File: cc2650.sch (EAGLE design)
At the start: 22 parts, among them IC4 CC2650MODAMOHR, SW1 SPST_TACT-KMR2, SW2 SPST_TACT-KMR2, U1 Value, U402 TPS62233DRY

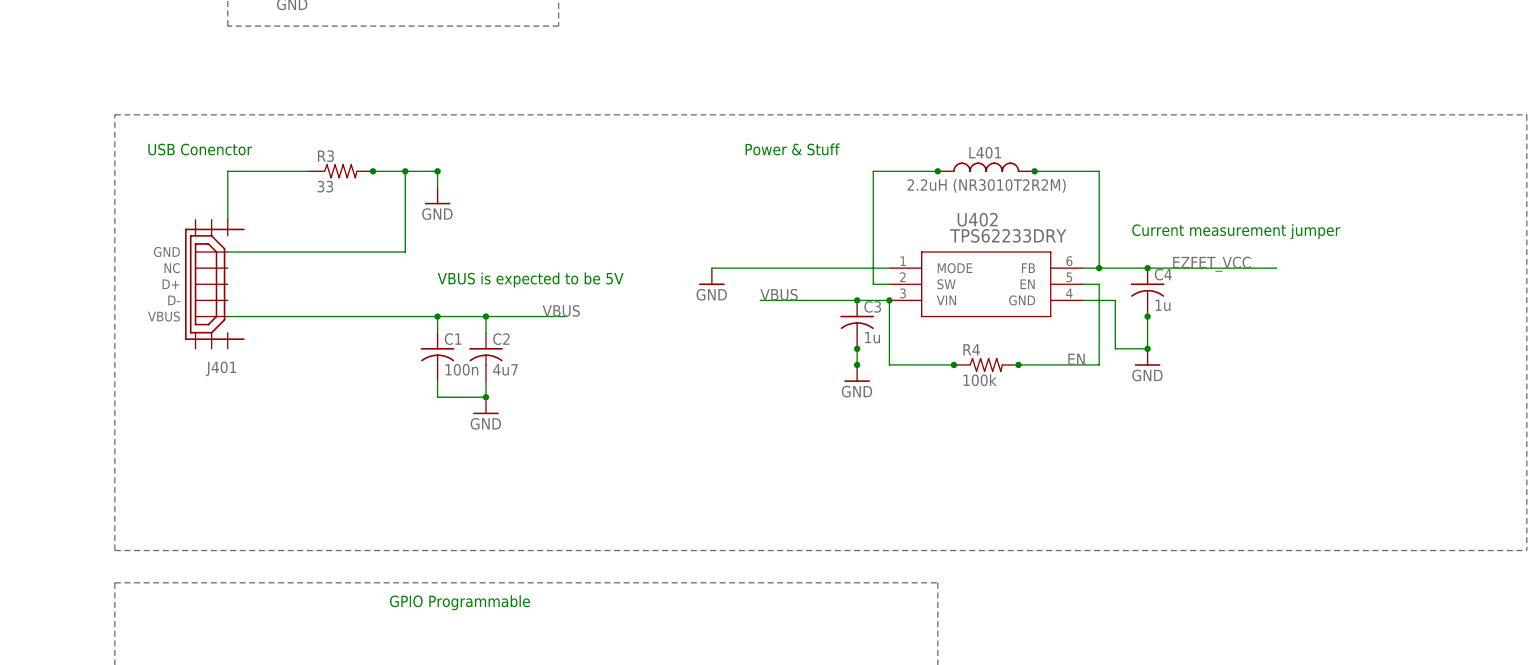
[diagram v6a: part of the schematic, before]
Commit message: Switched out USB connector.
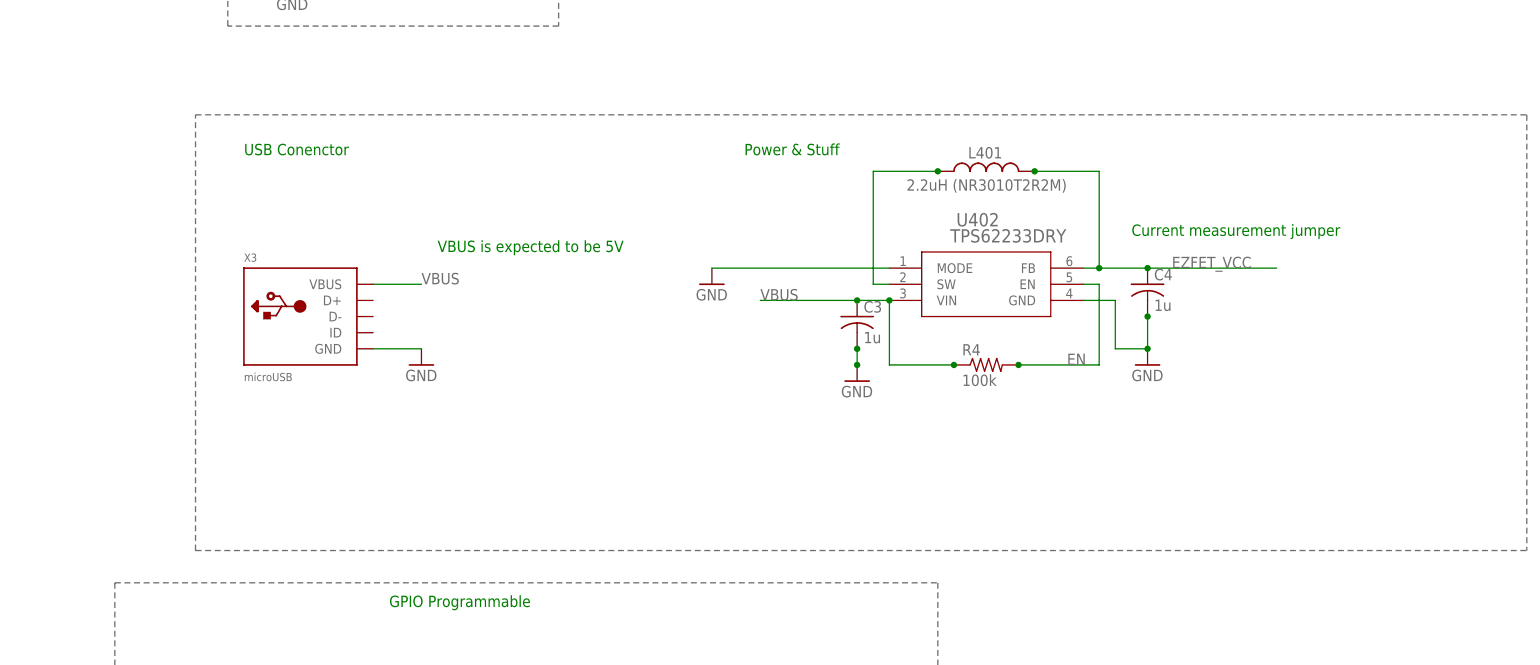
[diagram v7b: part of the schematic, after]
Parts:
- removed C1: 100n, adafruit:C-USC0402
- removed C2: 4u7, adafruit:C-USC1206
- removed J401: (no value), usb_con-update:USB_MICRO_FLIPPED
- removed R3: 33, adafruit:R-US_R0402
- added X3: microUSB, microbuilder:USB_MICRO_20329_V2
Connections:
- removed net N$1: J401.SHIELD1, R3.1
- net GND: now also X3.GND; no longer C1.2, C2.2, J401.GND, R3.2
- net VBUS: now also X3.VBUS; no longer C1.1, C2.1, J401.VBUS
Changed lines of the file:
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@@
 <attribute name="OC_NEWARK" value="05M0345"/>
 </part>
-<part name="GND56" library="supply1" deviceset="GND" device=""/>
-<part name="GND64" library="supply1" deviceset="GND" device=""/>
 <part name="U402" library="tps62231dry" deviceset="TPS6223X_DRY_6" device="" value="TPS62233DRY">
 <attribute name="MF" value=""/>
@@
 <part name="P+4" library="supply1" library_urn="urn:adsk.eagle:library:371" deviceset="VCC" device=""/>
 <part name="P+5" library="supply1" library_urn="urn:adsk.eagle:library:371" deviceset="VCC" device=""/>
-<part name="C1" library="adafruit" deviceset="C-US" device="C0402" value="100n">
-<attribute name="MF" value=""/>
-<attribute name="MPN" value="C1005X7R1H104K050BB"/>
-<attribute name="OC_NEWARK" value="04X3230"/>
-</part>
-<part name="C2" library="adafruit" deviceset="C-US" device="C1206" value="4u7">
-<attribute name="MF" value=""/>
-<attribute name="MPN" value="GRT31CC81E475KE01L"/>
-<attribute name="OC_NEWARK" value="01AC8998"/>
-</part>
 <part name="C3" library="adafruit" deviceset="C-US" device="C0805" value="1u">
 <attribute name="MF" value=""/>
@@
 <attribute name="MPN" value="CGA2B2C0G1H102J050BA"/>
 <attribute name="OC_NEWARK" value="04X3142"/>
-</part>
-<part name="R3" library="adafruit" deviceset="R-US_" device="R0402" value="33">
-<attribute name="MF" value=""/>
-<attribute name="MPN" value="ERJ-U02F33R0X"/>
-<attribute name="OC_NEWARK" value="51W3197"/>
 </part>
 <part name="R1" library="adafruit" deviceset="R-US_" device="R0402" value="47k">
@@
 </part>
 <part name="P+2" library="supply1" library_urn="urn:adsk.eagle:library:371" deviceset="VCC" device=""/>
-<part name="J401" library="usb_con-update" deviceset="USB_MICRO_FLIPPED" device="">
-<attribute name="MF" value=""/>
-<attribute name="MPN" value="ZX62R-B-5P(30)"/>
-<attribute name="OC_NEWARK" value="84Y6712"/>
-</part>
 <part name="GND6" library="supply1" library_urn="urn:adsk.eagle:library:371" deviceset="GND" device=""/>
 <part name="GND8" library="supply1" library_urn="urn:adsk.eagle:library:371" deviceset="GND" device=""/>
@@
 </part>
 <part name="U1" library="OPT3001" deviceset="OPT3001DNPR" device="" value="Value"/>
+<part name="X3" library="microbuilder" deviceset="USB" device="_MICRO_20329_V2" value="microUSB"/>
+<part name="GND4" library="supply1" library_urn="urn:adsk.eagle:library:371" deviceset="GND" device=""/>
 </parts>
 <sheets>
 <sheet>
 <plain>
-<text x="22.86" y="25.4" size="1.778" layer="91">USB Conenctor</text>
+<text x="38.1" y="25.4" size="1.778" layer="91">USB Conenctor</text>
 <text x="36.322" y="86.106" size="2.54" layer="95">RESET</text>
 <wire x1="35.56" y1="45.72" x2="35.56" y2="90.17" width="0.1524" layer="95" style="shortdash"/>
@@
 <text x="104.14" y="83.82" size="1.778" layer="91">Power LED w/ jumper</text>
 <text x="116.84" y="25.4" size="1.778" layer="91">Power &amp; Stuff</text>
-<text x="68.58" y="5.08" size="1.778" layer="91">VBUS is expected to be 5V</text>
+<text x="68.58" y="10.16" size="1.778" layer="91">VBUS is expected to be 5V</text>
 <text x="177.8" y="12.7" size="1.778" layer="91">Current measurement jumper</text>
-<wire x1="17.78" y1="-36.83" x2="17.78" y2="31.75" width="0.1524" layer="95" style="shortdash"/>
-<wire x1="17.78" y1="31.75" x2="240.03" y2="31.75" width="0.1524" layer="95" style="shortdash"/>
+<wire x1="30.48" y1="-36.83" x2="30.48" y2="31.75" width="0.1524" layer="95" style="shortdash"/>
+<wire x1="30.48" y1="31.75" x2="240.03" y2="31.75" width="0.1524" layer="95" style="shortdash"/>
 <wire x1="240.03" y1="31.75" x2="240.03" y2="-36.83" width="0.1524" layer="95" style="shortdash"/>
-<wire x1="17.78" y1="-36.83" x2="240.03" y2="-36.83" width="0.1524" layer="95" style="shortdash"/>
+<wire x1="30.48" y1="-36.83" x2="240.03" y2="-36.83" width="0.1524" layer="95" style="shortdash"/>
 <wire x1="17.78" y1="-92.71" x2="17.78" y2="-41.91" width="0.1524" layer="95" style="shortdash"/>
 <wire x1="17.78" y1="-41.91" x2="147.32" y2="-41.91" width="0.1524" layer="95" style="shortdash"/>
@@
 <attribute name="MPN" x="139.7" y="68.58" size="1.778" layer="96" display="off"/>
 </instance>
-<instance part="GND56" gate="1" x="68.58" y="17.78"/>
-<instance part="GND64" gate="1" x="76.2" y="-15.24"/>
 <instance part="U402" gate="&gt;NAME" x="139.7" y="7.62">
 <attribute name="OC_NEWARK" x="139.7" y="7.62" size="1.778" layer="96" display="off"/>
@@
 <instance part="P+4" gate="VCC" x="-17.78" y="7.62"/>
 <instance part="P+5" gate="VCC" x="45.72" y="83.82"/>
-<instance part="C1" gate="G$1" x="68.58" y="-5.08">
-<attribute name="OC_NEWARK" x="68.58" y="-5.08" size="1.778" layer="96" display="off"/>
-<attribute name="MF" x="68.58" y="-5.08" size="1.778" layer="96" display="off"/>
-<attribute name="MPN" x="68.58" y="-5.08" size="1.778" layer="96" display="off"/>
-</instance>
-<instance part="C2" gate="G$1" x="76.2" y="-5.08">
-<attribute name="OC_NEWARK" x="76.2" y="-5.08" size="1.778" layer="96" display="off"/>
-<attribute name="MF" x="76.2" y="-5.08" size="1.778" layer="96" display="off"/>
-<attribute name="MPN" x="76.2" y="-5.08" size="1.778" layer="96" display="off"/>
-</instance>
 <instance part="C3" gate="G$1" x="134.62" y="0">
 <attribute name="OC_NEWARK" x="134.62" y="0" size="1.778" layer="96" display="off"/>
@@
 <attribute name="MPN" x="45.72" y="63.5" size="1.778" layer="96" display="off"/>
 </instance>
-<instance part="R3" gate="G$1" x="53.34" y="22.86">
-<attribute name="OC_NEWARK" x="53.34" y="22.86" size="1.778" layer="96" display="off"/>
-<attribute name="MF" x="53.34" y="22.86" size="1.778" layer="96" display="off"/>
-<attribute name="MPN" x="53.34" y="22.86" size="1.778" layer="96" display="off"/>
-</instance>
 <instance part="R1" gate="G$1" x="45.72" y="73.66" rot="R270">
 <attribute name="OC_NEWARK" x="45.72" y="73.66" size="1.778" layer="96" display="off"/>
@@
 </instance>
 <instance part="P+2" gate="VCC" x="-134.62" y="48.26"/>
-<instance part="J401" gate="G$1" x="33.02" y="5.08" rot="R180">
-<attribute name="OC_NEWARK" x="33.02" y="5.08" size="1.778" layer="96" display="off"/>
-<attribute name="MF" x="33.02" y="5.08" size="1.778" layer="96" display="off"/>
-<attribute name="MPN" x="33.02" y="5.08" size="1.778" layer="96" display="off"/>
-</instance>
 <instance part="GND6" gate="1" x="-33.02" y="17.78"/>
 <instance part="GND8" gate="1" x="66.04" y="-68.58"/>
@@
 </instance>
 <instance part="U1" gate="A" x="-76.2" y="-88.9"/>
+<instance part="X3" gate="G$1" x="48.26" y="0"/>
+<instance part="GND4" gate="1" x="66.04" y="-7.62"/>
 </instances>
 <busses>
@@
 </segment>
 <segment>
-<pinref part="GND56" gate="1" pin="GND"/>
-<wire x1="68.58" y1="20.32" x2="68.58" y2="22.86" width="0.1524" layer="91"/>
-<wire x1="68.58" y1="22.86" x2="63.5" y2="22.86" width="0.1524" layer="91"/>
-<wire x1="58.42" y1="22.86" x2="63.5" y2="22.86" width="0.1524" layer="91"/>
-<wire x1="63.5" y1="22.86" x2="63.5" y2="10.16" width="0.1524" layer="91"/>
-<junction x="63.5" y="22.86"/>
-<wire x1="63.5" y1="10.16" x2="35.56" y2="10.16" width="0.1524" layer="91"/>
-<pinref part="R3" gate="G$1" pin="2"/>
-<junction x="58.42" y="22.86"/>
-<junction x="68.58" y="22.86"/>
-<pinref part="J401" gate="G$1" pin="GND"/>
-</segment>
-<segment>
-<pinref part="GND64" gate="1" pin="GND"/>
-<wire x1="76.2" y1="-10.16" x2="76.2" y2="-12.7" width="0.1524" layer="91"/>
-<wire x1="76.2" y1="-12.7" x2="68.58" y2="-12.7" width="0.1524" layer="91"/>
-<wire x1="68.58" y1="-12.7" x2="68.58" y2="-10.16" width="0.1524" layer="91"/>
-<junction x="76.2" y="-12.7"/>
-<pinref part="C1" gate="G$1" pin="2"/>
-<pinref part="C2" gate="G$1" pin="2"/>
-</segment>
-<segment>
 <pinref part="GND50" gate="1" pin="GND"/>
 <wire x1="134.62" y1="-5.08" x2="134.62" y2="-7.62" width="0.1524" layer="91"/>
@@
 <wire x1="53.34" y1="-60.96" x2="53.34" y2="-63.5" width="0.1524" layer="91"/>
 <junction x="53.34" y="-63.5"/>
+</segment>
+<segment>
+<pinref part="X3" gate="G$1" pin="GND"/>
+<pinref part="GND4" gate="1" pin="GND"/>
+<wire x1="58.42" y1="-5.08" x2="66.04" y2="-5.08" width="0.1524" layer="91"/>
 </segment>
 </net>
@@
 <net name="VBUS" class="2">
 <segment>
-<wire x1="68.58" y1="0" x2="68.58" y2="-2.54" width="0.1524" layer="91"/>
-<wire x1="68.58" y1="0" x2="76.2" y2="0" width="0.1524" layer="91"/>
-<wire x1="76.2" y1="0" x2="88.9" y2="0" width="0.1524" layer="91"/>
-<junction x="68.58" y="0"/>
-<wire x1="76.2" y1="0" x2="76.2" y2="-2.54" width="0.1524" layer="91"/>
-<junction x="76.2" y="0"/>
-<wire x1="35.56" y1="0" x2="68.58" y2="0" width="0.1524" layer="91"/>
-<pinref part="C1" gate="G$1" pin="1"/>
-<pinref part="C2" gate="G$1" pin="1"/>
-<label x="85.09" y="0" size="1.778" layer="95"/>
-<pinref part="J401" gate="G$1" pin="VBUS"/>
-</segment>
-<segment>
 <pinref part="U402" gate="&gt;NAME" pin="VIN"/>
 <wire x1="119.38" y1="2.54" x2="134.62" y2="2.54" width="0.1524" layer="91"/>
@@
 <label x="-121.92" y="50.8" size="1.778" layer="95"/>
 </segment>
-</net>
-<net name="N$1" class="0">
-<segment>
-<pinref part="R3" gate="G$1" pin="1"/>
-<pinref part="J401" gate="G$1" pin="SHIELD1"/>
-<wire x1="35.56" y1="15.24" x2="35.56" y2="22.86" width="0.1524" layer="91"/>
-<wire x1="35.56" y1="22.86" x2="48.26" y2="22.86" width="0.1524" layer="91"/>
-</segment>
-</net>
+<segment>
+<pinref part="X3" gate="G$1" pin="VBUS"/>
+<wire x1="58.42" y1="5.08" x2="66.04" y2="5.08" width="0.1524" layer="91"/>
+<label x="66.04" y="5.08" size="1.778" layer="95"/>
+</segment>
+</net>

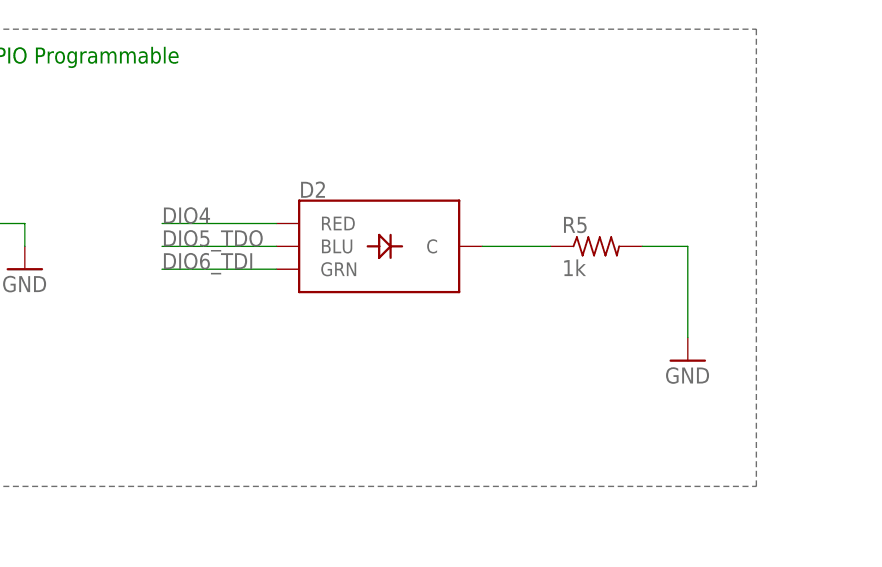
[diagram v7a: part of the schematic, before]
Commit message: Changed position of holes, fixed dimensions.
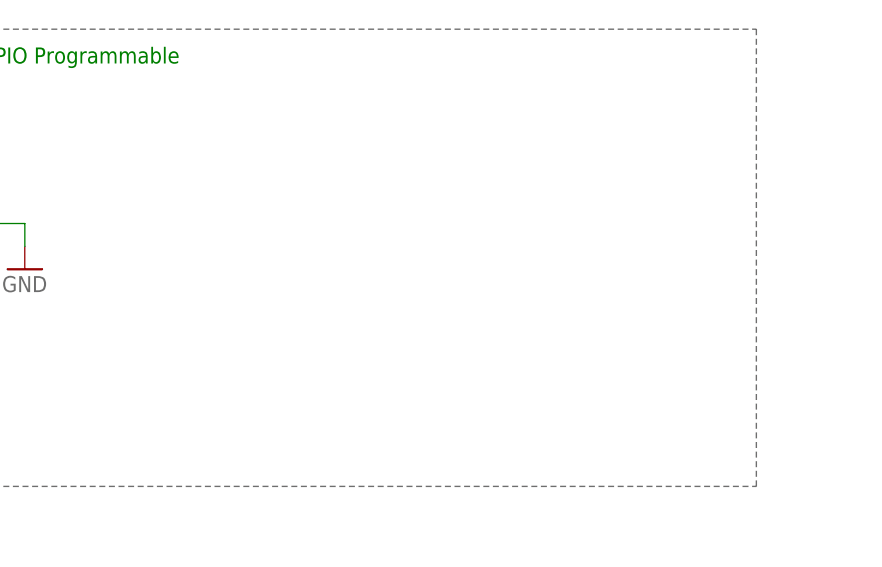
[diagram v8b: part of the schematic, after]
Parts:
- removed D2: (no value), SparkFun-LED:LED-RGB-CCPIRANHA
- removed R5: 1k, adafruit:R-US_R0402
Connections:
- removed net N$2: D2.C, R5.1
- net DIO4: no longer D2.RED
- net DIO5_TDO: no longer D2.BLU
- net DIO6_TDI: no longer D2.GRN
- net GND: no longer R5.2
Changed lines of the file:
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@@
 <attribute name="OC_NEWARK" value="87K4752"/>
-</part>
-<part name="GND5" library="supply1" library_urn="urn:adsk.eagle:library:371" deviceset="GND" device=""/>
-<part name="D2" library="SparkFun-LED" deviceset="LED-RGB-CC" device="PIRANHA">
-<attribute name="MF" value=""/>
-<attribute name="MPN" value="CLMVB-FKA-CFHEHLCBB7A363"/>
-<attribute name="OC_NEWARK" value="11X6434"/>
 </part>
 <part name="JP3" library="microbuilder" deviceset="HEADER-1X12" device="">
@@
 <part name="GND6" library="supply1" library_urn="urn:adsk.eagle:library:371" deviceset="GND" device=""/>
 <part name="GND8" library="supply1" library_urn="urn:adsk.eagle:library:371" deviceset="GND" device=""/>
-<part name="R5" library="adafruit" deviceset="R-US_" device="R0402" value="1k">
-<attribute name="MF" value=""/>
-<attribute name="MPN" value="ERA-2AEB471X"/>
-<attribute name="OC_NEWARK" value="08N2086"/>
-</part>
 <part name="U1" library="OPT3001" deviceset="OPT3001DNPR" device="" value="Value"/>
 <part name="X3" library="microbuilder" deviceset="USB" device="_MICRO_20329_V2" value="microUSB"/>
@@
 <attribute name="MPN" x="154.94" y="22.86" size="1.778" layer="96" display="off"/>
 </instance>
-<instance part="GND5" gate="1" x="139.7" y="-78.74"/>
-<instance part="D2" gate="G$1" x="104.14" y="-66.04">
-<attribute name="OC_NEWARK" x="104.14" y="-66.04" size="1.778" layer="96" display="off"/>
-<attribute name="MF" x="104.14" y="-66.04" size="1.778" layer="96" display="off"/>
-<attribute name="MPN" x="104.14" y="-66.04" size="1.778" layer="96" display="off"/>
-</instance>
 <instance part="JP3" gate="G$1" x="-91.44" y="35.56">
 <attribute name="OC_NEWARK" x="-91.44" y="35.56" size="1.778" layer="96" display="off"/>
@@
 <instance part="GND6" gate="1" x="-33.02" y="17.78"/>
 <instance part="GND8" gate="1" x="66.04" y="-68.58"/>
-<instance part="R5" gate="G$1" x="129.54" y="-66.04">
-<attribute name="OC_NEWARK" x="129.54" y="-66.04" size="1.778" layer="96" display="off"/>
-<attribute name="MF" x="129.54" y="-66.04" size="1.778" layer="96" display="off"/>
-<attribute name="MPN" x="129.54" y="-66.04" size="1.778" layer="96" display="off"/>
-</instance>
 <instance part="U1" gate="A" x="-76.2" y="-88.9"/>
 <instance part="X3" gate="G$1" x="48.26" y="0"/>
@@
 </segment>
 <segment>
-<pinref part="GND5" gate="1" pin="GND"/>
-<wire x1="139.7" y1="-66.04" x2="139.7" y2="-76.2" width="0.1524" layer="91"/>
-<pinref part="R5" gate="G$1" pin="2"/>
-<wire x1="134.62" y1="-66.04" x2="139.7" y2="-66.04" width="0.1524" layer="91"/>
-</segment>
-<segment>
 <pinref part="GND6" gate="1" pin="GND"/>
 <wire x1="-33.02" y1="20.32" x2="-33.02" y2="22.86" width="0.1524" layer="91"/>
@@
 <label x="-121.92" y="27.94" size="1.778" layer="95"/>
 </segment>
-<segment>
-<pinref part="D2" gate="G$1" pin="BLU"/>
-<wire x1="93.98" y1="-66.04" x2="81.28" y2="-66.04" width="0.1524" layer="91"/>
-<label x="81.28" y="-66.04" size="1.778" layer="95"/>
-</segment>
 </net>
 <net name="DIO6_TDI" class="0">
@@
 <wire x1="-93.98" y1="30.48" x2="-121.92" y2="30.48" width="0.1524" layer="91"/>
 <label x="-121.92" y="30.48" size="1.778" layer="95"/>
-</segment>
-<segment>
-<pinref part="D2" gate="G$1" pin="GRN"/>
-<wire x1="93.98" y1="-68.58" x2="81.28" y2="-68.58" width="0.1524" layer="91"/>
-<label x="81.28" y="-68.58" size="1.778" layer="95"/>
 </segment>
 </net>
@@
 <wire x1="-93.98" y1="25.4" x2="-121.92" y2="25.4" width="0.1524" layer="91"/>
 <label x="-121.92" y="25.4" size="1.778" layer="95"/>
-</segment>
-<segment>
-<pinref part="D2" gate="G$1" pin="RED"/>
-<wire x1="93.98" y1="-63.5" x2="81.28" y2="-63.5" width="0.1524" layer="91"/>
-<label x="81.28" y="-63.5" size="1.778" layer="95"/>
 </segment>
 </net>
@@
 </segment>
 </net>
-<net name="N$2" class="0">
-<segment>
-<pinref part="D2" gate="G$1" pin="C"/>
-<pinref part="R5" gate="G$1" pin="1"/>
-<wire x1="116.84" y1="-66.04" x2="124.46" y2="-66.04" width="0.1524" layer="91"/>
-</segment>
-</net>
